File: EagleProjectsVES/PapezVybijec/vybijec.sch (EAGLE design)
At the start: 28 parts

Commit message: PapezVybijec: - hotova dps
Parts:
- P1: value (none) -> COLLECTOR
- P2: value (none) -> BASE
- P3: value (none) -> EMITTER
- P4: value (none) -> GROUND
- P5: value (none) -> COL
- P6: value (none) -> EMIT
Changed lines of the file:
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@@
 <part name="GND5" library="supply1" deviceset="GND" device=""/>
 <part name="GND6" library="supply1" deviceset="GND" device=""/>
-<part name="P1" library="PADs" deviceset="PAD" device="" technology="PAD3MM"/>
-<part name="P2" library="PADs" deviceset="PAD" device="" technology="PAD3MM"/>
-<part name="P3" library="PADs" deviceset="PAD" device="" technology="PAD3MM"/>
-<part name="P4" library="PADs" deviceset="PAD" device="" technology="PAD3MM"/>
-<part name="P5" library="PADs" deviceset="PAD" device="" technology="PAD3MM"/>
-<part name="P6" library="PADs" deviceset="PAD" device="" technology="PAD3MM"/>
+<part name="P1" library="PADs" deviceset="PAD" device="" technology="PAD3MM" value="COLLECTOR"/>
+<part name="P2" library="PADs" deviceset="PAD" device="" technology="PAD3MM" value="BASE"/>
+<part name="P3" library="PADs" deviceset="PAD" device="" technology="PAD3MM" value="EMITTER"/>
+<part name="P4" library="PADs" deviceset="PAD" device="" technology="PAD3MM" value="GROUND"/>
+<part name="P5" library="PADs" deviceset="PAD" device="" technology="PAD3MM" value="COL"/>
+<part name="P6" library="PADs" deviceset="PAD" device="" technology="PAD3MM" value="EMIT"/>
 <part name="GND7" library="supply1" deviceset="GND" device=""/>
 <part name="P+1" library="supply1" deviceset="VCC" device=""/>

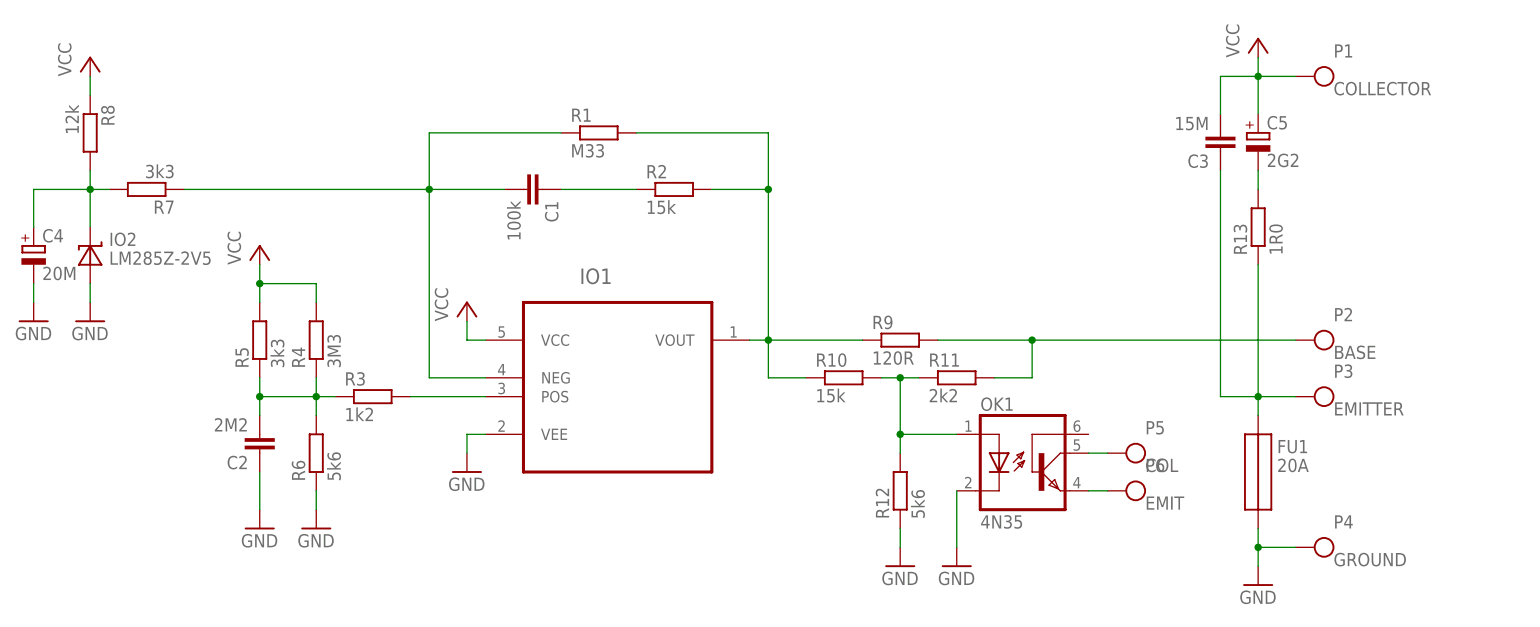
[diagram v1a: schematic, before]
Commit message: gitignore: - pridany knihovny
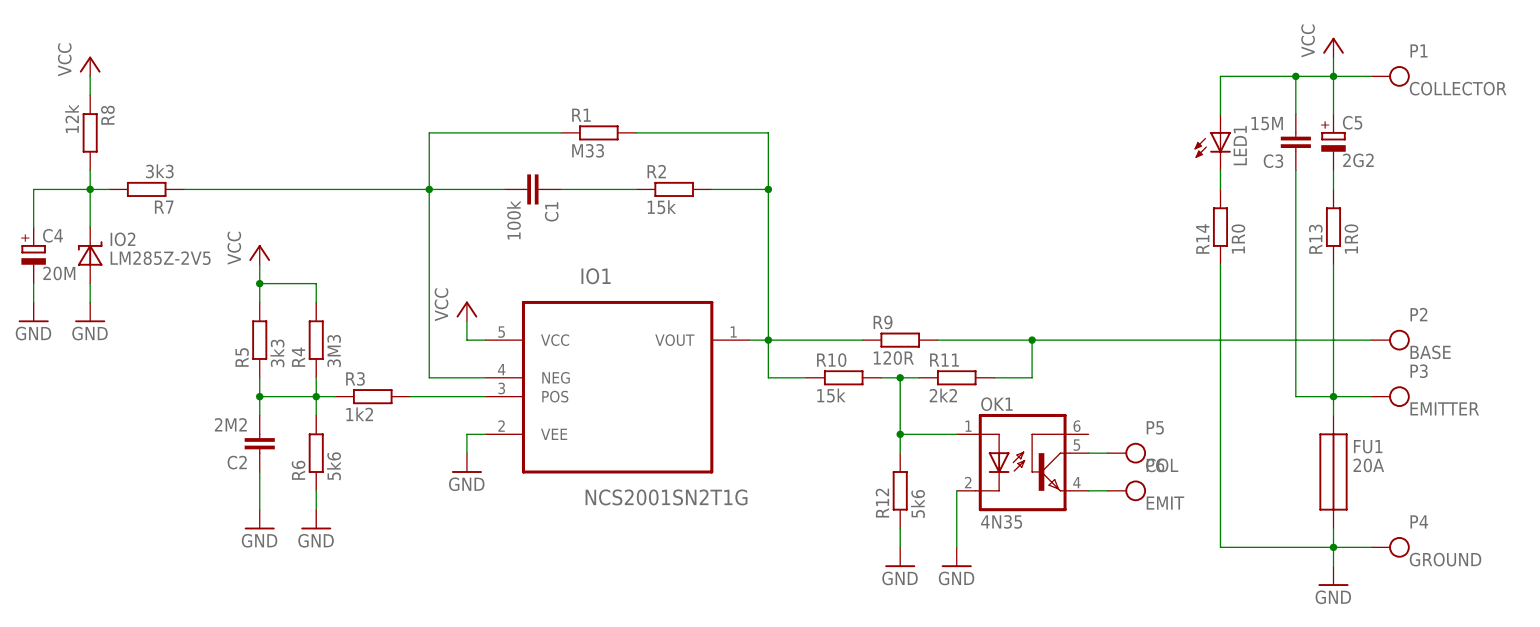
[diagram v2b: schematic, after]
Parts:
- added LED1: (no value), adafruit:LED3MM
- added R14: 1R0, rcl:R-EU_0207/10
- IO1: value (none) -> NCS2001SN2T1G
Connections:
- new net N$12: LED1.C, R14.2
- net GND: now also R14.1
- net VCC: now also LED1.A
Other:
- moved on the sheet: C3, C5, FU1, P1, P2, P3, P4, R13

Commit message: PapezVybijec: - opraveny rozmery nytu
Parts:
- P5, P6: device PADs:PADPAD3MM -> PADs:PADPAD1.6MM
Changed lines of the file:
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@@
 <part name="GND5" library="supply1" deviceset="GND" device=""/>
 <part name="GND6" library="supply1" deviceset="GND" device=""/>
-<part name="P1" library="PADs" deviceset="PAD" device="" technology="PAD3MM" value="COLLECTOR"/>
-<part name="P2" library="PADs" deviceset="PAD" device="" technology="PAD3MM" value="BASE"/>
-<part name="P3" library="PADs" deviceset="PAD" device="" technology="PAD3MM" value="EMITTER"/>
-<part name="P4" library="PADs" deviceset="PAD" device="" technology="PAD3MM" value="GROUND"/>
-<part name="P5" library="PADs" deviceset="PAD" device="" technology="PAD3MM" value="COL"/>
-<part name="P6" library="PADs" deviceset="PAD" device="" technology="PAD3MM" value="EMIT"/>
+<part name="P1" library="PADs" deviceset="PAD" device="PAD3MM" value="COLLECTOR"/>
+<part name="P2" library="PADs" deviceset="PAD" device="PAD3MM" value="BASE"/>
+<part name="P3" library="PADs" deviceset="PAD" device="PAD3MM" value="EMITTER"/>
+<part name="P4" library="PADs" deviceset="PAD" device="PAD3MM" value="GROUND"/>
+<part name="P5" library="PADs" deviceset="PAD" device="PAD1.6MM" value="COL"/>
+<part name="P6" library="PADs" deviceset="PAD" device="PAD1.6MM" value="EMIT"/>
 <part name="GND7" library="supply1" deviceset="GND" device=""/>
 <part name="P+1" library="supply1" deviceset="VCC" device=""/>

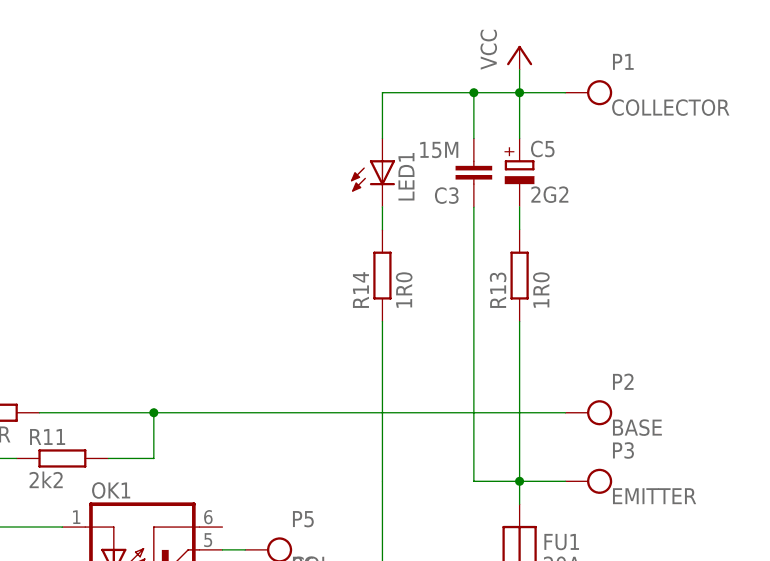
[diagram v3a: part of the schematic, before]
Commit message: PapezVybijec: - hotove podklady, - pridany navrhove pravidla
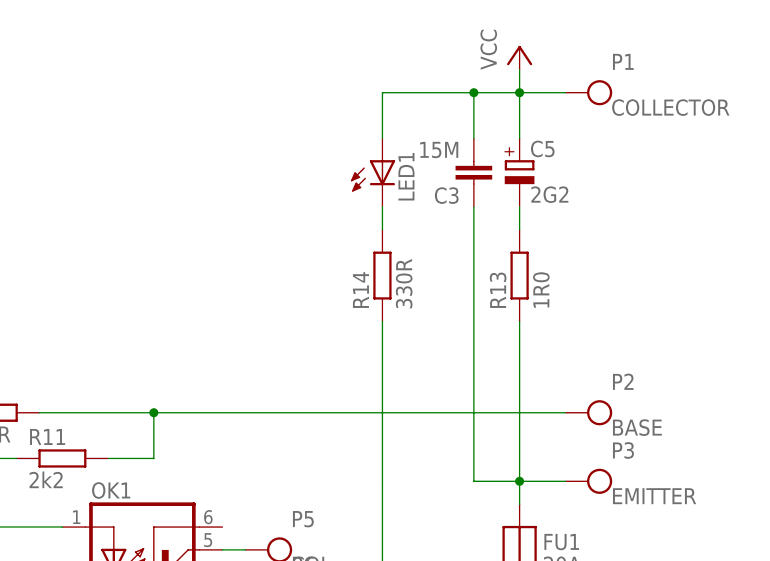
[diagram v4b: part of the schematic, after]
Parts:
- R14: value 1R0 -> 330R
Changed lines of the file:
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@@
 <grid distance="0.1" unitdist="inch" unit="inch" style="lines" multiple="1" display="no" altdistance="0.01" altunitdist="inch" altunit="inch"/>
 <layers>
-<layer number="1" name="Top" color="4" fill="1" visible="yes" active="no"/>
-<layer number="2" name="Route2" color="1" fill="3" visible="yes" active="no"/>
-<layer number="3" name="Route3" color="4" fill="3" visible="yes" active="no"/>
-<layer number="4" name="Route4" color="1" fill="4" visible="yes" active="no"/>
-<layer number="5" name="Route5" color="4" fill="4" visible="yes" active="no"/>
-<layer number="6" name="Route6" color="1" fill="8" visible="yes" active="no"/>
-<layer number="7" name="Route7" color="4" fill="8" visible="yes" active="no"/>
-<layer number="8" name="Route8" color="1" fill="2" visible="yes" active="no"/>
-<layer number="9" name="Route9" color="4" fill="2" visible="yes" active="no"/>
-<layer number="10" name="Route10" color="1" fill="7" visible="yes" active="no"/>
-<layer number="11" name="Route11" color="4" fill="7" visible="yes" active="no"/>
-<layer number="12" name="Route12" color="1" fill="5" visible="yes" active="no"/>
-<layer number="13" name="Route13" color="4" fill="5" visible="yes" active="no"/>
-<layer number="14" name="Route14" color="1" fill="6" visible="yes" active="no"/>
-<layer number="15" name="Route15" color="4" fill="6" visible="yes" active="no"/>
-<layer number="16" name="Bottom" color="1" fill="1" visible="yes" active="no"/>
-<layer number="17" name="Pads" color="2" fill="1" visible="yes" active="no"/>
-<layer number="18" name="Vias" color="2" fill="1" visible="yes" active="no"/>
-<layer number="19" name="Unrouted" color="6" fill="1" visible="yes" active="no"/>
-<layer number="20" name="Dimension" color="15" fill="1" visible="yes" active="no"/>
-<layer number="21" name="tPlace" color="7" fill="1" visible="yes" active="no"/>
-<layer number="22" name="bPlace" color="7" fill="1" visible="yes" active="no"/>
-<layer number="23" name="tOrigins" color="15" fill="1" visible="yes" active="no"/>
-<layer number="24" name="bOrigins" color="15" fill="1" visible="yes" active="no"/>
-<layer number="25" name="tNames" color="7" fill="1" visible="yes" active="no"/>
-<layer number="26" name="bNames" color="7" fill="1" visible="yes" active="no"/>
-<layer number="27" name="tValues" color="7" fill="1" visible="yes" active="no"/>
-<layer number="28" name="bValues" color="7" fill="1" visible="yes" active="no"/>
+<layer number="1" name="Top" color="4" fill="1" visible="no" active="no"/>
+<layer number="2" name="Route2" color="1" fill="3" visible="no" active="no"/>
+<layer number="3" name="Route3" color="4" fill="3" visible="no" active="no"/>
+<layer number="4" name="Route4" color="1" fill="4" visible="no" active="no"/>
+<layer number="5" name="Route5" color="4" fill="4" visible="no" active="no"/>
+<layer number="6" name="Route6" color="1" fill="8" visible="no" active="no"/>
+<layer number="7" name="Route7" color="4" fill="8" visible="no" active="no"/>
+<layer number="8" name="Route8" color="1" fill="2" visible="no" active="no"/>
+<layer number="9" name="Route9" color="4" fill="2" visible="no" active="no"/>
+<layer number="10" name="Route10" color="1" fill="7" visible="no" active="no"/>
+<layer number="11" name="Route11" color="4" fill="7" visible="no" active="no"/>
+<layer number="12" name="Route12" color="1" fill="5" visible="no" active="no"/>
+<layer number="13" name="Route13" color="4" fill="5" visible="no" active="no"/>
+<layer number="14" name="Route14" color="1" fill="6" visible="no" active="no"/>
+<layer number="15" name="Route15" color="4" fill="6" visible="no" active="no"/>
+<layer number="16" name="Bottom" color="1" fill="1" visible="no" active="no"/>
+<layer number="17" name="Pads" color="2" fill="1" visible="no" active="no"/>
+<layer number="18" name="Vias" color="2" fill="1" visible="no" active="no"/>
+<layer number="19" name="Unrouted" color="6" fill="1" visible="no" active="no"/>
+<layer number="20" name="Dimension" color="15" fill="1" visible="no" active="no"/>
+<layer number="21" name="tPlace" color="7" fill="1" visible="no" active="no"/>
+<layer number="22" name="bPlace" color="7" fill="1" visible="no" active="no"/>
+<layer number="23" name="tOrigins" color="15" fill="1" visible="no" active="no"/>
+<layer number="24" name="bOrigins" color="15" fill="1" visible="no" active="no"/>
+<layer number="25" name="tNames" color="7" fill="1" visible="no" active="no"/>
+<layer number="26" name="bNames" color="7" fill="1" visible="no" active="no"/>
+<layer number="27" name="tValues" color="7" fill="1" visible="no" active="no"/>
+<layer number="28" name="bValues" color="7" fill="1" visible="no" active="no"/>
 <layer number="29" name="tStop" color="7" fill="3" visible="no" active="no"/>
 <layer number="30" name="bStop" color="7" fill="6" visible="no" active="no"/>
@@
 <layer number="35" name="tGlue" color="7" fill="4" visible="no" active="no"/>
 <layer number="36" name="bGlue" color="7" fill="5" visible="no" active="no"/>
-<layer number="37" name="tTest" color="7" fill="1" visible="yes" active="no"/>
-<layer number="38" name="bTest" color="7" fill="1" visible="yes" active="no"/>
+<layer number="37" name="tTest" color="7" fill="1" visible="no" active="no"/>
+<layer number="38" name="bTest" color="7" fill="1" visible="no" active="no"/>
 <layer number="39" name="tKeepout" color="4" fill="11" visible="no" active="no"/>
 <layer number="40" name="bKeepout" color="1" fill="11" visible="no" active="no"/>
@@
 <layer number="44" name="Drills" color="7" fill="1" visible="no" active="no"/>
 <layer number="45" name="Holes" color="7" fill="1" visible="no" active="no"/>
-<layer number="46" name="Milling" color="3" fill="1" visible="yes" active="no"/>
-<layer number="47" name="Measures" color="7" fill="1" visible="yes" active="no"/>
-<layer number="48" name="Document" color="7" fill="1" visible="yes" active="no"/>
-<layer number="49" name="Reference" color="7" fill="1" visible="yes" active="no"/>
-<layer number="50" name="dxf" color="7" fill="1" visible="yes" active="no"/>
-<layer number="51" name="tDocu" color="7" fill="1" visible="yes" active="no"/>
-<layer number="52" name="bDocu" color="7" fill="1" visible="yes" active="no"/>
-<layer number="53" name="tGND_GNDA" color="7" fill="9" visible="yes" active="no"/>
-<layer number="54" name="bGND_GNDA" color="1" fill="9" visible="yes" active="no"/>
-<layer number="56" name="wert" color="7" fill="1" visible="yes" active="no"/>
-<layer number="57" name="tCAD" color="7" fill="1" visible="yes" active="no"/>
-<layer number="59" name="tCarbon" color="7" fill="1" visible="yes" active="no"/>
-<layer number="60" name="bCarbon" color="7" fill="1" visible="yes" active="no"/>
+<layer number="46" name="Milling" color="3" fill="1" visible="no" active="no"/>
+<layer number="47" name="Measures" color="7" fill="1" visible="no" active="no"/>
+<layer number="48" name="Document" color="7" fill="1" visible="no" active="no"/>
+<layer number="49" name="Reference" color="7" fill="1" visible="no" active="no"/>
+<layer number="50" name="dxf" color="7" fill="1" visible="no" active="no"/>
+<layer number="51" name="tDocu" color="7" fill="1" visible="no" active="no"/>
+<layer number="52" name="bDocu" color="7" fill="1" visible="no" active="no"/>
+<layer number="53" name="tGND_GNDA" color="7" fill="9" visible="no" active="no"/>
+<layer number="54" name="bGND_GNDA" color="1" fill="9" visible="no" active="no"/>
+<layer number="56" name="wert" color="7" fill="1" visible="no" active="no"/>
+<layer number="57" name="tCAD" color="7" fill="1" visible="no" active="no"/>
+<layer number="59" name="tCarbon" color="7" fill="1" visible="no" active="no"/>
+<layer number="60" name="bCarbon" color="7" fill="1" visible="no" active="no"/>
 <layer number="90" name="Modules" color="5" fill="1" visible="yes" active="yes"/>
 <layer number="91" name="Nets" color="2" fill="1" visible="yes" active="yes"/>
@@
 <part name="FU1" library="pojistka" deviceset="POJISTKA" device="" value="20A"/>
 <part name="LED1" library="adafruit" deviceset="LED" device="3MM"/>
-<part name="R14" library="rcl" deviceset="R-EU_" device="0207/10" value="1R0"/>
+<part name="R14" library="rcl" deviceset="R-EU_" device="0207/10" value="330R"/>
 </parts>
 <sheets>
